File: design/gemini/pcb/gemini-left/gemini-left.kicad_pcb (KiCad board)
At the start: 2 copper layers, 128.6 x 84.2 mm, 49 parts, among them J1 USB-C link, SW00 Tab, SW01 Q, SW02 W, SW03 E, SW04 R, SW05 T, SW10 Esc/Ctrl, SW11 A, SW12 S, SW13 D, SW14 F, SW15 G, SW20 Shift, SW21 Z, SW22 X, SW23 C, SW24 V, SW25 B, SW30 Ctrl, SW31 GUI, SW32 Alt, SW33 Space, U1 Raspberry Pi Pico

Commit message: add LEDs
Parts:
- added LED00: SK6812MINI-E, LED_SK6812MINI-E_3.2x2.8mm_P1.5mm_ReverseMount, B.Cu at (11.9, 14.6)
- added LED01: SK6812MINI-E, LED_SK6812MINI-E_3.2x2.8mm_P1.5mm_ReverseMount, B.Cu at (33.3, 14.6)
- added LED02: SK6812MINI-E, LED_SK6812MINI-E_3.2x2.8mm_P1.5mm_ReverseMount, B.Cu at (52.4, 14.6)
- added LED03: SK6812MINI-E, LED_SK6812MINI-E_3.2x2.8mm_P1.5mm_ReverseMount, B.Cu at (71.4, 14.6)
- added LED04: SK6812MINI-E, LED_SK6812MINI-E_3.2x2.8mm_P1.5mm_ReverseMount, B.Cu at (90.5, 14.6)
- added LED05: SK6812MINI-E, LED_SK6812MINI-E_3.2x2.8mm_P1.5mm_ReverseMount, B.Cu at (109.5, 14.6)
- added LED10: SK6812MINI-E, LED_SK6812MINI-E_3.2x2.8mm_P1.5mm_ReverseMount, B.Cu at (14.3, 33.7)
- added LED11: SK6812MINI-E, LED_SK6812MINI-E_3.2x2.8mm_P1.5mm_ReverseMount, B.Cu at (38.1, 33.7)
- added LED12: SK6812MINI-E, LED_SK6812MINI-E_3.2x2.8mm_P1.5mm_ReverseMount, B.Cu at (57.1, 33.7)
- added LED13: SK6812MINI-E, LED_SK6812MINI-E_3.2x2.8mm_P1.5mm_ReverseMount, B.Cu at (76.2, 33.7)
- added LED14: SK6812MINI-E, LED_SK6812MINI-E_3.2x2.8mm_P1.5mm_ReverseMount, B.Cu at (95.2, 33.7)
- added LED15: SK6812MINI-E, LED_SK6812MINI-E_3.2x2.8mm_P1.5mm_ReverseMount, B.Cu at (114.3, 33.7)
- added LED20: SK6812MINI-E, LED_SK6812MINI-E_3.2x2.8mm_P1.5mm_ReverseMount, B.Cu at (16.7, 52.7)
- added LED21: SK6812MINI-E, LED_SK6812MINI-E_3.2x2.8mm_P1.5mm_ReverseMount, B.Cu at (42.9, 52.7)
- added LED22: SK6812MINI-E, LED_SK6812MINI-E_3.2x2.8mm_P1.5mm_ReverseMount, B.Cu at (61.9, 52.7)
- added LED23: SK6812MINI-E, LED_SK6812MINI-E_3.2x2.8mm_P1.5mm_ReverseMount, B.Cu at (81.0, 52.7)
- added LED24: SK6812MINI-E, LED_SK6812MINI-E_3.2x2.8mm_P1.5mm_ReverseMount, B.Cu at (100.0, 52.7)
- added LED25: SK6812MINI-E, LED_SK6812MINI-E_3.2x2.8mm_P1.5mm_ReverseMount, B.Cu at (119.1, 52.7)
- added LED30: SK6812MINI-E, LED_SK6812MINI-E_3.2x2.8mm_P1.5mm_ReverseMount, B.Cu at (11.9, 71.8)
- added LED31: SK6812MINI-E, LED_SK6812MINI-E_3.2x2.8mm_P1.5mm_ReverseMount, B.Cu at (33.3, 71.8)
- added LED32: SK6812MINI-E, LED_SK6812MINI-E_3.2x2.8mm_P1.5mm_ReverseMount, B.Cu at (54.8, 71.8)
- added LED33: SK6812MINI-E, LED_SK6812MINI-E_3.2x2.8mm_P1.5mm_ReverseMount, B.Cu at (92.9, 71.8)
- added U2: 74AHCT1G125, SOT-23-5, B.Cu at (70.0, -4.00)
- moved D10 44.6 mm to (30.0, -4.00)
- moved D12 41.5 mm to (42.0, -4.00)
- moved D11 40.0 mm to (36.0, -4.00)
- moved U1 23.2 mm to (26.0, 28.6)
- moved D13 0.60 mm to (72.2, 36.6)
- moved D14 0.60 mm to (91.2, 36.6)
- moved D15 0.60 mm to (110.3, 36.6)
- moved D20 0.60 mm to (12.7, 55.6)
- moved D21 0.60 mm to (38.9, 55.6)
- moved D22 0.60 mm to (57.9, 55.6)
- moved D23 0.60 mm to (77.0, 55.6)
- moved D24 0.60 mm to (96.0, 55.6)
- moved D25 0.60 mm to (115.1, 55.6)
- moved D00 0.60 mm to (7.91, 17.5)
- moved D01 0.60 mm to (29.3, 17.5)
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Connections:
- J1 pad 10: (no net) -> LED_LINK
- J1 pad 11: +3V3 -> +5V
- J1 pad 2: +3V3 -> +5V
- J1 pad 3: (no net) -> LED_LINK
- J1 pad 4: (no net) -> LED_LINK
- J1 pad 9: (no net) -> LED_LINK
- U1 pad 21: (no net) -> LED_DATA
- U1 pad 40: (no net) -> +5V

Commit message: add usb c
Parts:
- added DV1: B5819W, D_SOD-123, B.Cu at (100.0, -4.00)
- added J2: USB-C host, HRO-TYPE-C-31-M-12-Assembly, B.Cu at (88.0, -3.50)
- added R3: 5k1, R_0603_1608Metric, B.Cu at (81.0, -1.00)
- added R4: 5k1, R_0603_1608Metric, B.Cu at (95.0, -1.00)
- added TP1: USB_DP, TestPoint_THTPad_D1.5mm_Drill0.7mm, B.Cu at (5.00, -1.50)
- added TP2: USB_DM, TestPoint_THTPad_D1.5mm_Drill0.7mm, B.Cu at (10.0, -1.50)
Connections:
- J1 pad 11: +5V -> VSYS
- J1 pad 2: +5V -> VSYS
- LED00 pad 1: +5V -> VSYS
- LED01 pad 1: +5V -> VSYS
- LED02 pad 1: +5V -> VSYS
- LED03 pad 1: +5V -> VSYS
- LED04 pad 1: +5V -> VSYS
- LED05 pad 1: +5V -> VSYS
- LED10 pad 1: +5V -> VSYS
- LED11 pad 1: +5V -> VSYS
- LED12 pad 1: +5V -> VSYS
- LED13 pad 1: +5V -> VSYS
- LED14 pad 1: +5V -> VSYS
- LED15 pad 1: +5V -> VSYS
- LED20 pad 1: +5V -> VSYS
- LED21 pad 1: +5V -> VSYS
- LED22 pad 1: +5V -> VSYS
- LED23 pad 1: +5V -> VSYS
- LED24 pad 1: +5V -> VSYS
- LED25 pad 1: +5V -> VSYS
- LED30 pad 1: +5V -> VSYS
- LED31 pad 1: +5V -> VSYS
- LED32 pad 1: +5V -> VSYS
- LED33 pad 1: +5V -> VSYS
- U1 pad 39: (no net) -> VSYS
- U1 pad 40: +5V -> (no net)
- U2 pad 5: +5V -> VSYS

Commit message: move usb c to the left
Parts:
- moved R4 78.6 mm to (16.5, -5.50)
- moved J2 78.5 mm to (9.50, -3.50)
- moved DV1 78.0 mm to (22.0, -5.50)
- moved R3 64.5 mm to (16.5, -1.50)
- moved TP1 16.5 mm to (21.5, -1.50)
- moved TP2 16.0 mm to (26.0, -1.50)

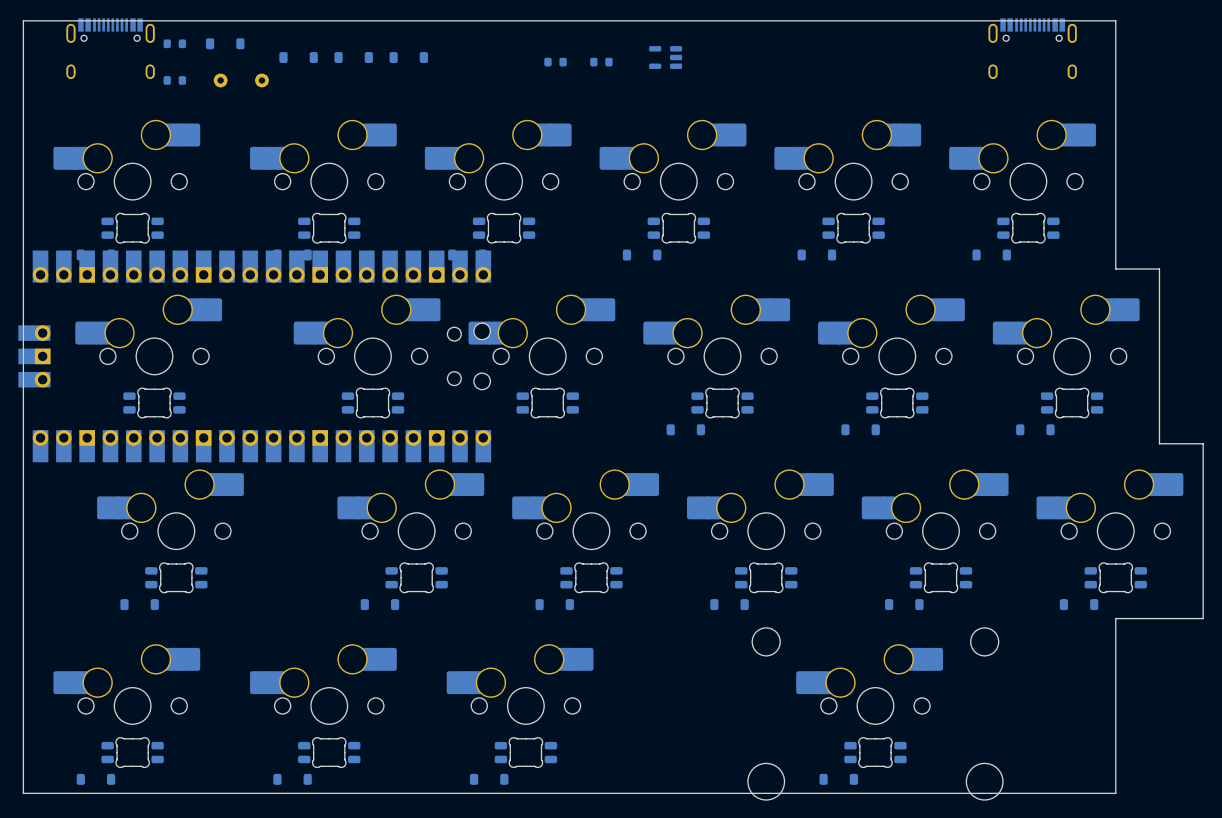
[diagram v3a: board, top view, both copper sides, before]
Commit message: add frontplate browline cover, add joining wall edges
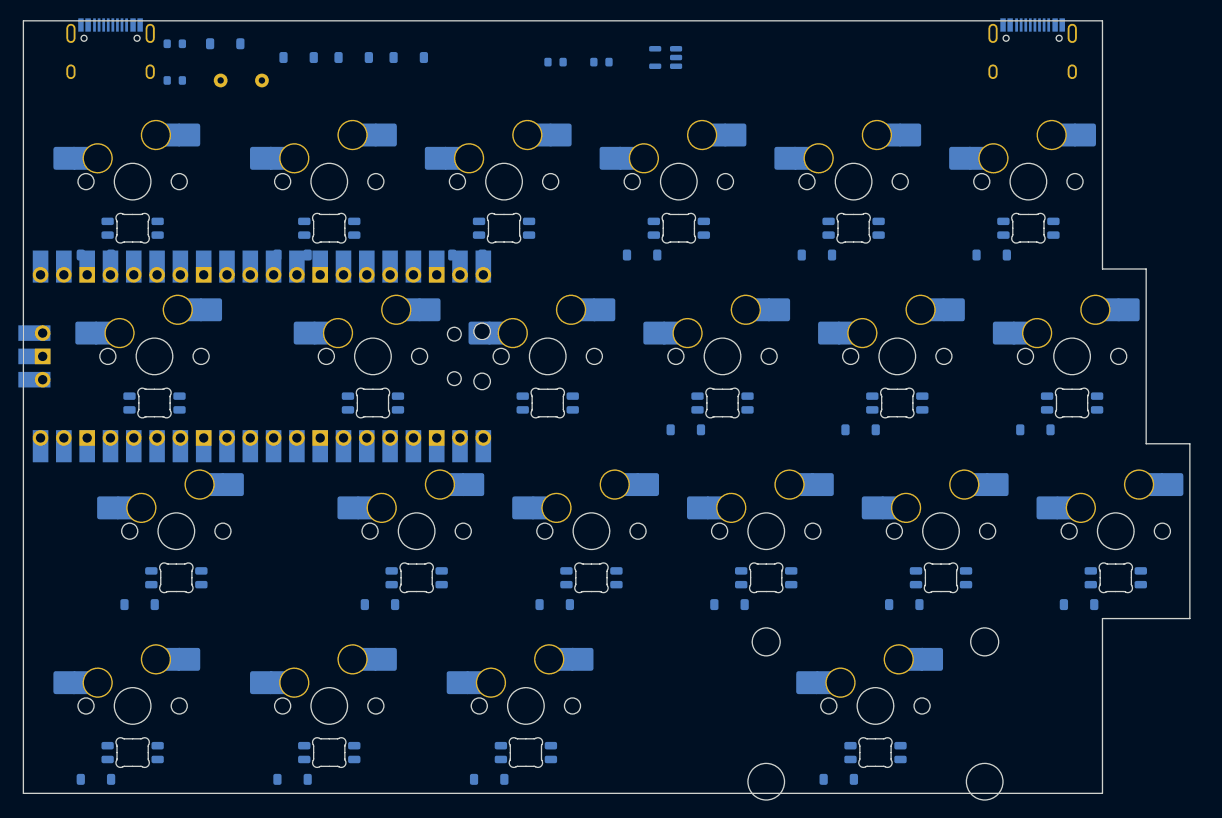
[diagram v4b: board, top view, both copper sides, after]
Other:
- board size 128.6 x 84.2 mm -> 127.1 x 84.2 mm

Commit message: a bunch of fixes
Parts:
- moved D00 45.5 mm to (48.0, -4.00)
- moved D02 35.0 mm to (76.0, -4.00)
- moved D01 32.7 mm to (54.0, -4.00)
- moved U1 1.00 mm to (26.0, 27.6)
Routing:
- net GND: track 0.00 -> 734.4 mm, vias 0 -> 6
- net VSYS: track 0.00 -> 672.9 mm, vias 0 -> 17
- net ROW1: track 0.00 -> 186.2 mm, vias 0 -> 4
- net ROW2: track 0.00 -> 151.2 mm, vias 0 -> 4
- net COL5: track 0.00 -> 150.9 mm
- net ROW0: track 0.00 -> 147.1 mm
- net ROW3: track 0.00 -> 140.9 mm, vias 0 -> 6
- net COL3: track 0.00 -> 140.4 mm, vias 0 -> 4
- net LED_CH18: track 0.00 -> 140.4 mm, vias 0 -> 2
- net LED_CH06: track 0.00 -> 138.4 mm, vias 0 -> 2
- net COL1: track 0.00 -> 134.1 mm, vias 0 -> 3
- net SCL: track 0.00 -> 130.2 mm, vias 0 -> 7
- net COL4: track 0.00 -> 128.1 mm, vias 0 -> 1
- net LED_CH12: track 0.00 -> 123.5 mm, vias 0 -> 2
- net SDA: track 0.00 -> 118.8 mm, vias 0 -> 3
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- added copper zone on B.Cu, net GND

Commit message: add silkscreening, and layer visibility for model view
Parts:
- added G1: Logo_Gemini, Logo_Gemini, F.Cu at (58.8, -4.00)
